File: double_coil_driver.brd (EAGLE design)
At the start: 100 x 50 mm, 57 parts, among them Q1 MOSFET-N, Q3 IRF7493, U2 V_REG_LDOSMD, U3 LT3750EMSPBF, X1 COIL

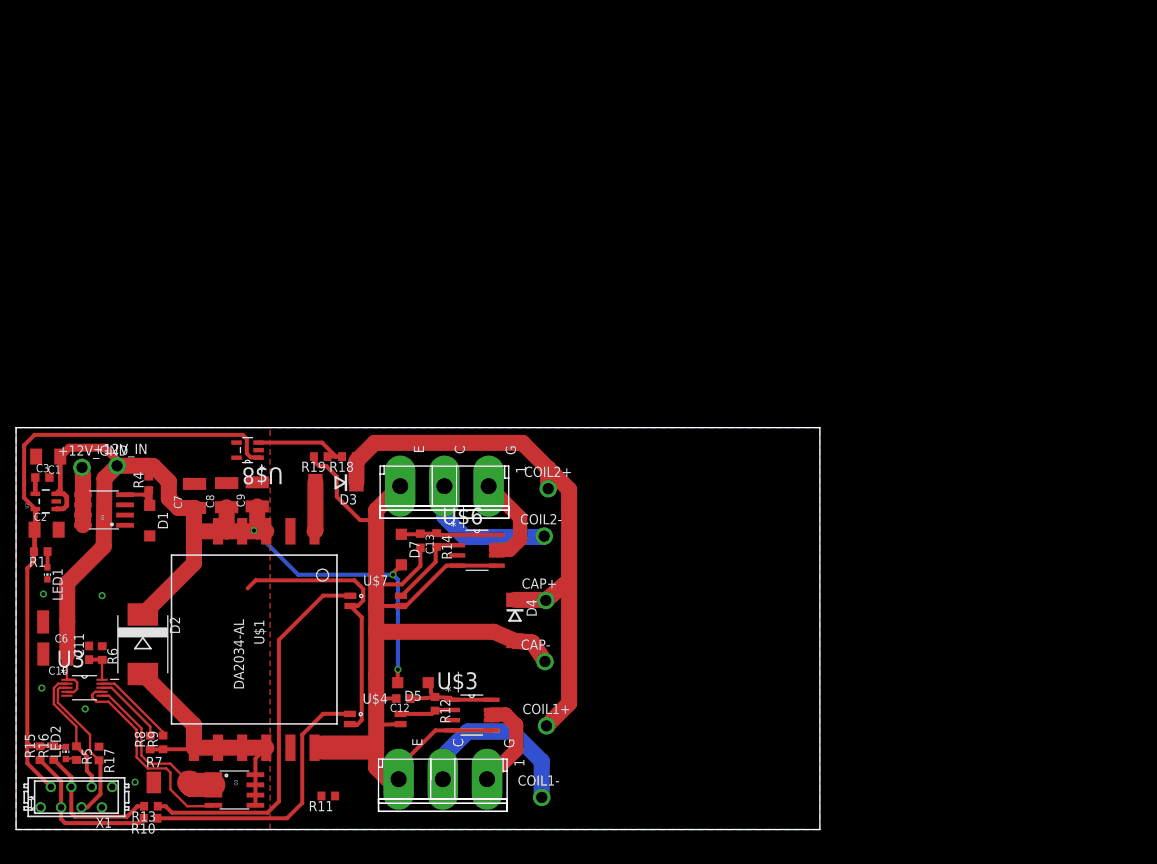
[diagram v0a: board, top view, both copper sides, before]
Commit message: Added opamp to ADC, changed board layout a bit
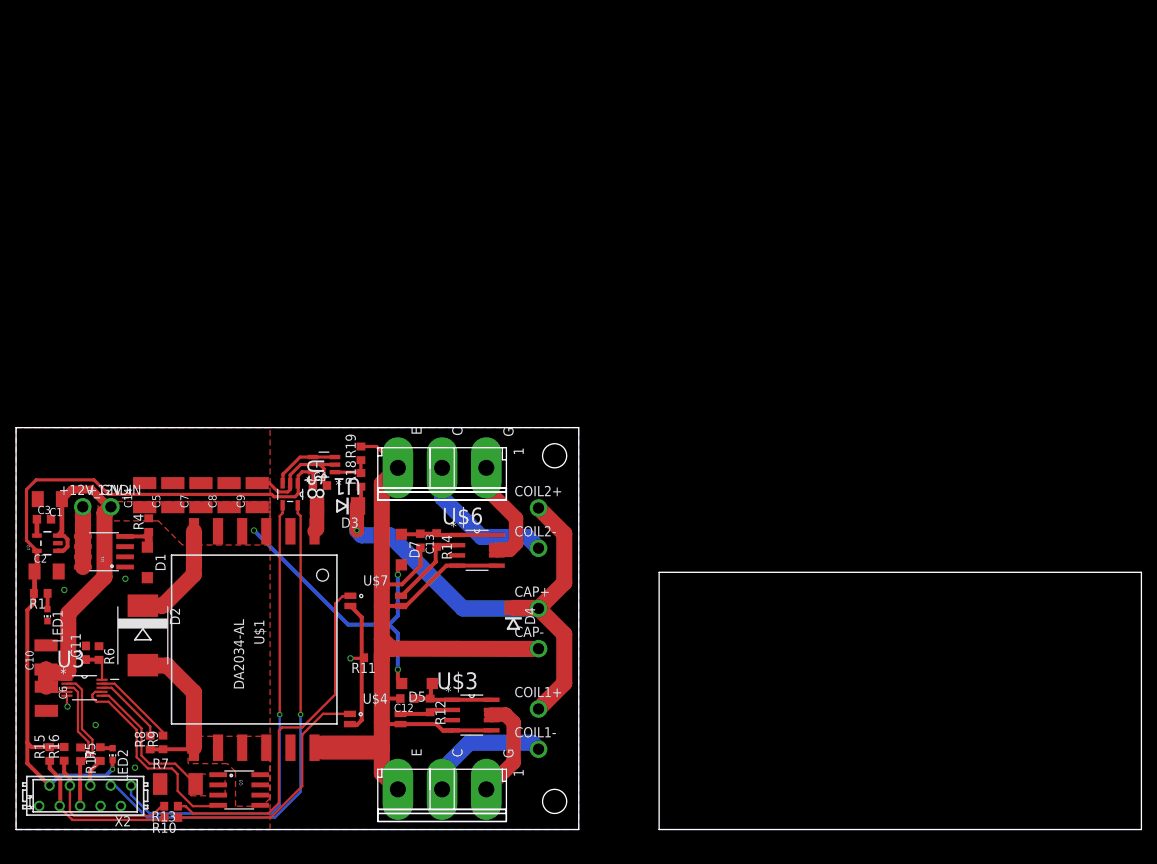
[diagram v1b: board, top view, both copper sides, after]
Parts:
- removed X1: COIL, con-amp-micromatch:MICROMATCH-8
- added C14, C5: (no value), rcl:C1210K
- added C4: 100nF, rcl:C0603K
- added U1: MCP6L01UT-E/OT, opamp-MCP6L01U:SOT95P270X145-5N
- added X2: MICROMATCH-10, con-amp-micromatch:MICROMATCH-10
- C11: value (none) -> 100pF
- R18: value 82k -> 8.2M
- R19: value 1k -> 59k
- moved R11 18.0 mm to (44.1, 21.4)
- moved C6 9.62 mm to (3.77, 16.3), turned to 270 degrees
- moved U$8 7.64 mm to (34.1, 41.7), turned to 270 degrees
- moved COIL1- 6.01 mm to (65.0, 10.0)
- moved LED2 5.82 mm to (12.0, 9.37), turned to 180 degrees
- moved C1 5.30 mm to (4.20, 41.1)
- moved D1 5.21 mm to (16.3, 33.2)
- moved U2 5.20 mm to (3.90, 35.6)
- moved C3 5.20 mm to (3.47, 38.6)
- moved R4 5.20 mm to (16.5, 37.9)
- moved LED1 5.20 mm to (3.90, 26.7)
- moved R1 5.20 mm to (3.07, 29.4)
- moved C2 5.20 mm to (3.80, 32.1)
- moved Q1 5.20 mm to (10.9, 34.6)
- moved +12V_IN 5.16 mm to (11.8, 40.1)
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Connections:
- new net N$5: U$8.3, U1.3, U1.4
- net +12V: now also C14.1, C5.1
- net +5V: now also C4.1, U1.5, X2.2; no longer X1.2
- net CHARGE: now also X2.5; no longer X1.5
- net DONE: now also X2.6; no longer X1.6
- net GNDA: now also C14.2, C4.2, C5.2, U1.2, X2.1, X2.7, X2.9; no longer X1.1
- net KICK1: now also X2.3; no longer X1.3
- net KICK2: now also X2.4; no longer X1.4
- net N$3: now also U1.1; no longer U$8.3
- net SCL: now also X2.8; no longer X1.8
- net SDA: now also X2.10; no longer X1.7
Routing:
- net SCL: track 0.00 -> 62.4 mm, vias 0 -> 1
- net SDA: track 0.00 -> 58.5 mm, vias 0 -> 1
- net +12V: track 130.9 -> 98.5 mm
- net AGND: track 135.5 -> 118.3 mm
- net N$13: track 34.1 -> 20.2 mm
- net +5V: track 81.9 -> 94.9 mm, vias 0 -> 1
- net N$5: track 0.00 -> 8.50 mm
- net N$15: track 73.7 -> 65.9 mm, vias 0 -> 1
- net N$3: track 12.1 -> 5.25 mm
- net N$16: track 22.5 -> 16.1 mm
- net N$10: track 23.0 -> 18.2 mm
- net N$19: track 34.3 -> 30.4 mm
- net N$14: track 6.10 -> 3.28 mm
- net CHARGE: track 19.5 -> 17.1 mm
- net N$26: track 47.3 -> 45.0 mm
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- added copper zone on layer 1, net +12V
- added copper zone on layer 1, net N$10
- added copper zone on layer 1, net N$13
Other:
- board size 100 x 50 mm -> 140 x 50 mm

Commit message: Changed board layout
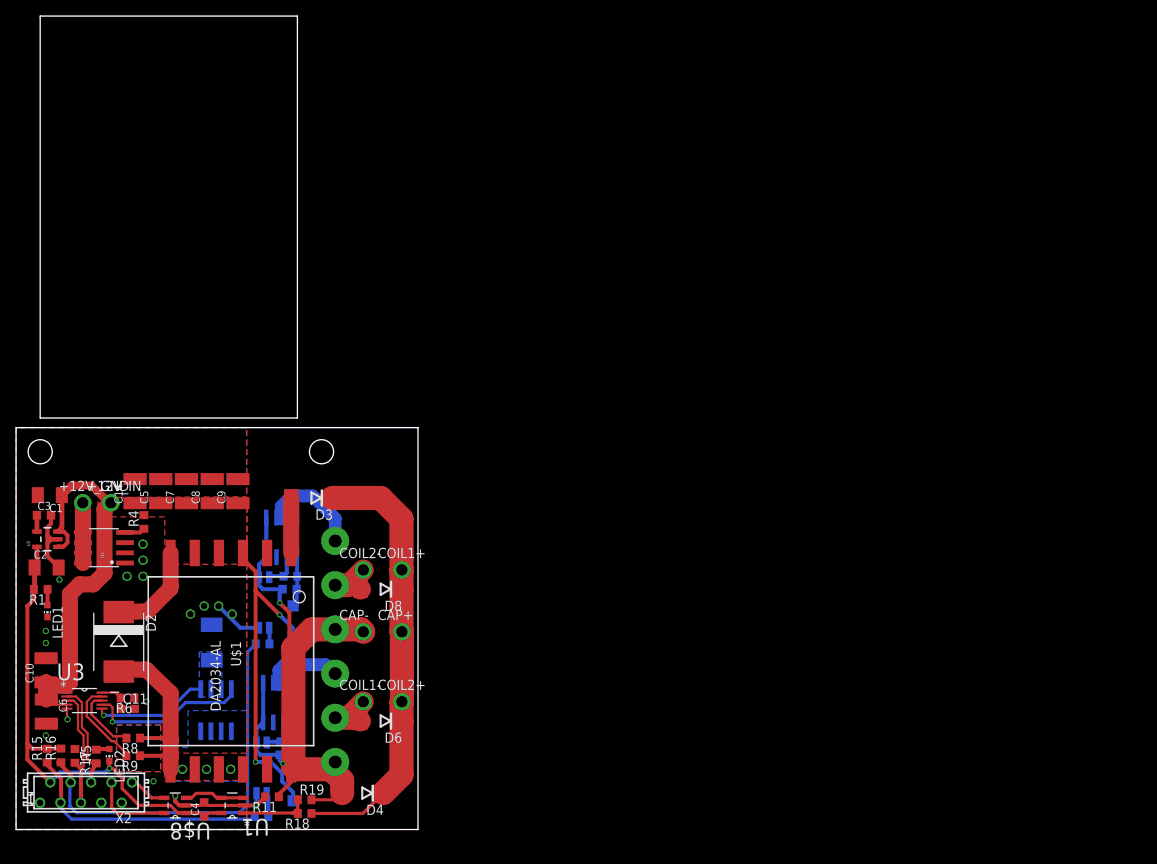
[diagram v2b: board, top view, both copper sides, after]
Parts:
- removed D1: (no value), diode:SOD123
- added D6, D8: MURS140, diode:DO214AA
- U$2, U$5: device to-247_n-channel_igbt:TO-247 -> to-247_n-channel_igbt-modified-pads:TO-247
- moved U1 43.9 mm to (26.9, 3.00)
- moved R19 43.7 mm to (35.9, 3.70), turned to 0 degrees
- moved C4 42.8 mm to (23.4, 2.50), turned to 90 degrees
- moved R18 42.1 mm to (35.9, 2.00), turned to 180 degrees
- moved U$8 41.3 mm to (19.8, 3.00), turned to 180 degrees
- moved COIL2+ 29.5 mm to (48.0, 15.9)
- moved D4 27.8 mm to (43.1, 4.53), turned to 180 degrees
- moved U$6 24.4 mm to (33.0, 36.4), flipped to the bottom, turned to 90 degrees
- moved COIL1+ 24.3 mm to (48.0, 32.3)
- moved U$3 24.1 mm to (32.6, 15.8), flipped to the bottom, turned to 90 degrees
- moved R13 23.2 mm to (30.7, 23.1), flipped to the bottom, turned to 0 degrees
- moved COIL1- 22.6 mm to (43.2, 15.9)
- moved COIL2- 22.0 mm to (43.2, 32.3)
- moved CAP- 21.9 mm to (43.2, 24.6)
- moved R11 21.2 mm to (31.8, 4.08)
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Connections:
- net GNDA: no longer D1.A
- net N$15: now also D6.C, D8.C
- net N$16: now also D6.A
- net N$23: now also D8.A
- net N$7: no longer D1.C
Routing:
- net SDA: track 58.5 -> 4.81 mm, vias 1 -> 0
- net SCL: track 62.4 -> 9.97 mm, vias 1 -> 0
- net N$26: track 45.0 -> 2.01 mm
- net AGND: track 118.3 -> 79.8 mm, vias 0 -> 2
- net +5V: track 94.9 -> 61.9 mm
- net KICK2: track 19.1 -> 49.7 mm
- net N$19: track 30.4 -> 2.97 mm
- net N$23: track 18.3 -> 6.08 mm
- net KICK1: track 20.2 -> 31.4 mm
- net N$15: track 65.9 -> 54.8 mm, vias 1 -> 0
- net N$16: track 16.1 -> 7.51 mm
- net +12V: track 98.5 -> 104.9 mm, vias 3 -> 2
- net N$25: track 10.6 -> 4.37 mm
- net N$6: track 26.2 -> 20.2 mm, vias 0 -> 1
- net N$13: track 20.2 -> 26.1 mm, vias 0 -> 3
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- added copper zone on layer 16, net N$10
- added copper zone on layer 16, net N$13
- added copper zone on layer 1, net N$20
- added copper zone on layer 16, net N$22
- removed copper zone on layer 1, net N$10
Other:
- board size 140 x 50 mm -> 50 x 101.2 mm

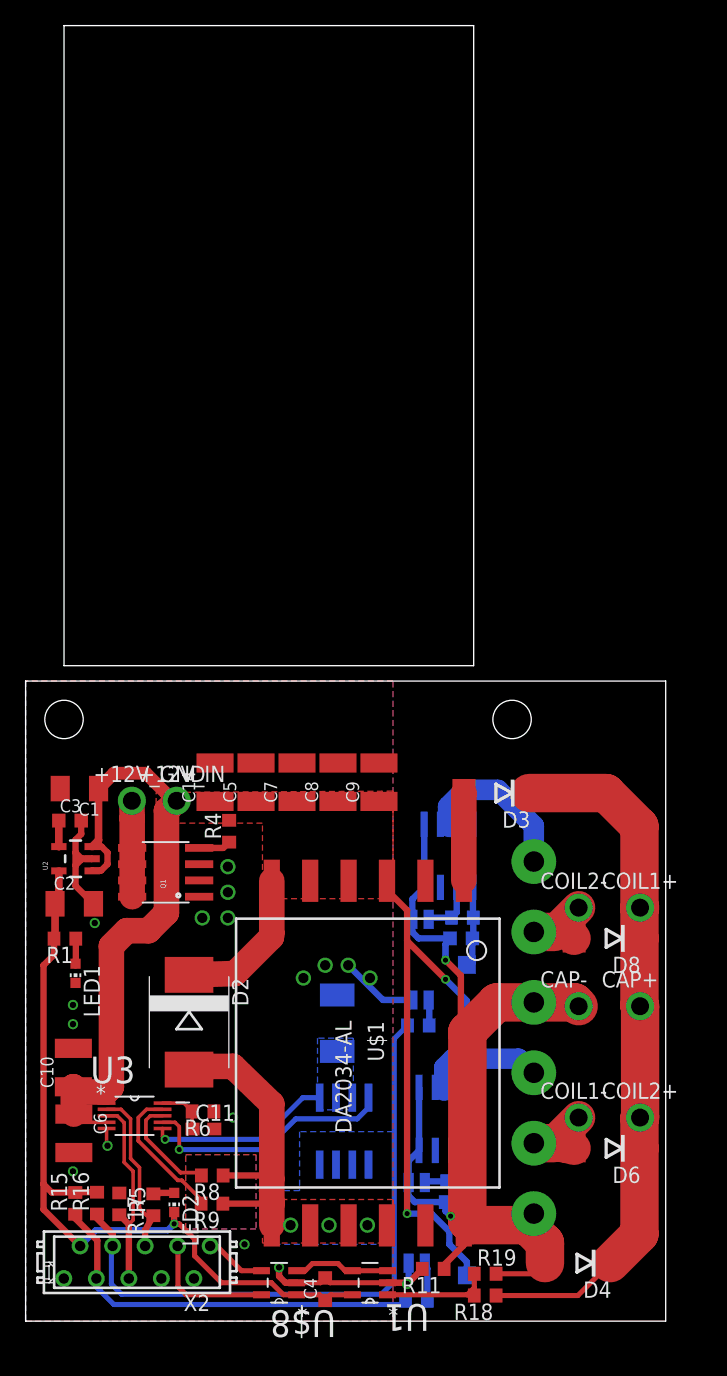
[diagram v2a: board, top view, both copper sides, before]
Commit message: Added MicroMatch hole and some labels
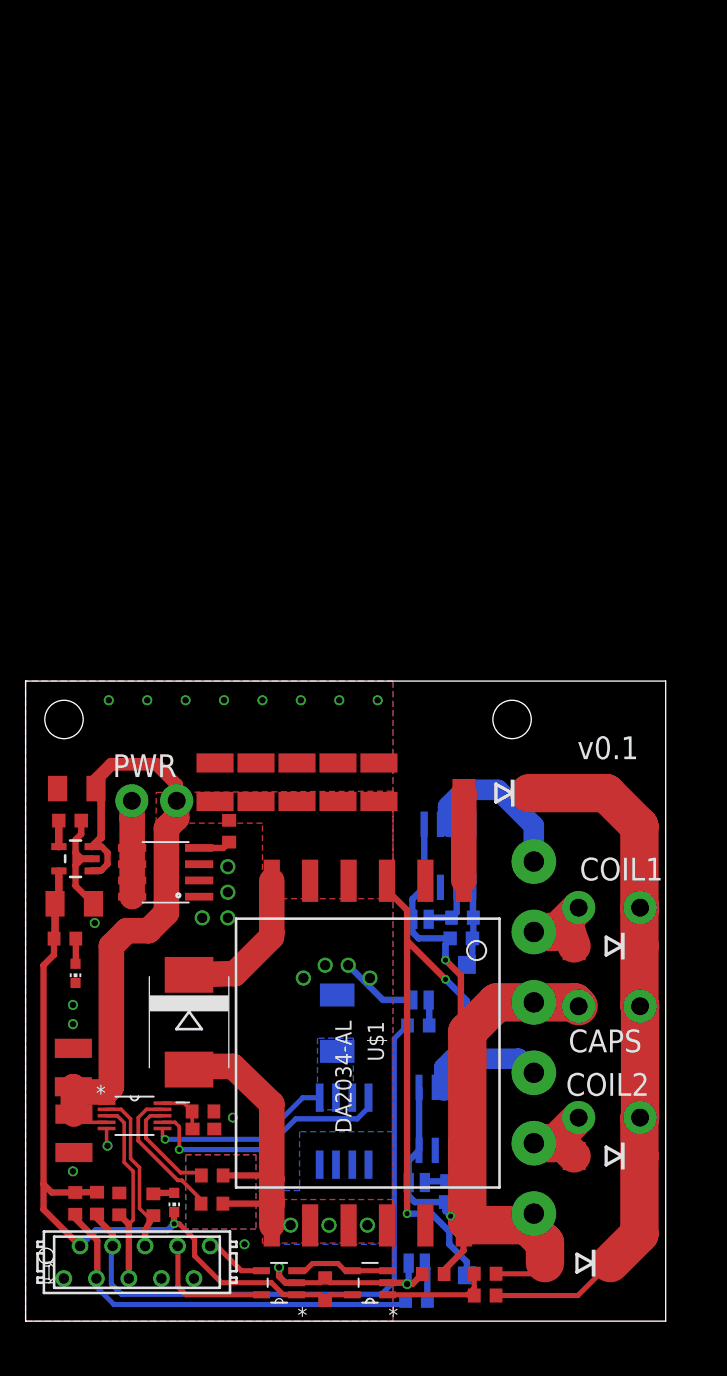
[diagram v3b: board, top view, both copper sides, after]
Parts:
- moved D6 0.60 mm to (45.4, 12.9)
- moved D8 0.60 mm to (45.4, 29.3)
- moved R11 0.40 mm to (31.8, 3.68)
- moved C1 0.20 mm to (4.00, 41.6)
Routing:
- net +12V: track 104.9 -> 107.1 mm
- net N$23: track 6.08 -> 6.61 mm
- net GNDA: track 32.5 -> 32.3 mm, vias 17 -> 25
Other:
- board size 50 x 101.2 mm -> 50 x 50 mm
- board text added: "CAPS"
- board text added: "COIL1"
- board text added: "COIL2"
- board text added: "PWR"
- board text added: "v0.1"

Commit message: Added missing capacitor values
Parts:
- C14, C5, C7, C8, C9: value (none) -> 10uF
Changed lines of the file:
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@@
 <attribute name="VALUE" x="40.1" y="30.1" size="1.27" layer="27" align="center-left"/>
 </element>
-<element name="C7" library="rcl" package="C1210K" value="" x="21.2" y="42.1" smashed="yes" rot="R90">
+<element name="C7" library="rcl" package="C1210K" value="10uF" x="21.2" y="42.1" smashed="yes" rot="R90">
 <attribute name="NAME" x="19.65" y="40.5" size="1.016" layer="27" rot="R90"/>
 <attribute name="VALUE" x="23.775" y="40.5" size="1.016" layer="27" rot="R90"/>
 </element>
-<element name="C8" library="rcl" package="C1210K" value="" x="24.4" y="42.1" smashed="yes" rot="R90">
+<element name="C8" library="rcl" package="C1210K" value="10uF" x="24.4" y="42.1" smashed="yes" rot="R90">
 <attribute name="NAME" x="22.85" y="40.5" size="1.016" layer="27" rot="R90"/>
 <attribute name="VALUE" x="26.975" y="40.5" size="1.016" layer="27" rot="R90"/>
 </element>
-<element name="C9" library="rcl" package="C1210K" value="" x="27.6" y="42.1" smashed="yes" rot="R90">
+<element name="C9" library="rcl" package="C1210K" value="10uF" x="27.6" y="42.1" smashed="yes" rot="R90">
 <attribute name="NAME" x="26.05" y="40.5" size="1.016" layer="27" rot="R90"/>
 <attribute name="VALUE" x="30.175" y="40.5" size="1.016" layer="27" rot="R90"/>
@@
 <attribute name="VALUE" x="25.05" y="1.7" size="1.016" layer="27" rot="R90"/>
 </element>
-<element name="C5" library="rcl" package="C1210K" value="" x="18" y="42.1" smashed="yes" rot="R90">
+<element name="C5" library="rcl" package="C1210K" value="10uF" x="18" y="42.1" smashed="yes" rot="R90">
 <attribute name="NAME" x="16.45" y="40.5" size="1.016" layer="27" rot="R90"/>
 <attribute name="VALUE" x="20.575" y="40.5" size="1.016" layer="27" rot="R90"/>
 </element>
-<element name="C14" library="rcl" package="C1210K" value="" x="14.8" y="42.1" smashed="yes" rot="R90">
+<element name="C14" library="rcl" package="C1210K" value="10uF" x="14.8" y="42.1" smashed="yes" rot="R90">
 <attribute name="NAME" x="13.25" y="40.5" size="1.016" layer="27" rot="R90"/>
 <attribute name="VALUE" x="17.375" y="40.5" size="1.016" layer="27" rot="R90"/>
